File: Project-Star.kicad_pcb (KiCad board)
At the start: 2 copper layers, 95 parts, among them J1 Motor Driver Header, J10 Leg3 Motor1, J11 Leg4 Motor3, J12 Leg4 Motor2, J13 Leg4 Motor1, J14 Leg5 Motor3, J15 Leg5 Motor2, J16 Leg5 Motor1, J17 Leg6 Motor3, J18 Leg6 Motor2, J19 Leg6 Motor1, J2 Leg1 Motor3, J3 Leg1 Motor2, J4 Leg1 Motor1, J5 Leg2 Motor3, J6 Leg2 Motor2, J7 Leg2 Motor1, J8 Leg3 Motor3, J9 Leg3 Motor2, U1 PCA9685PW, U2 PCA9685PW, U3 LMR51625DDC, U4 LMR51450

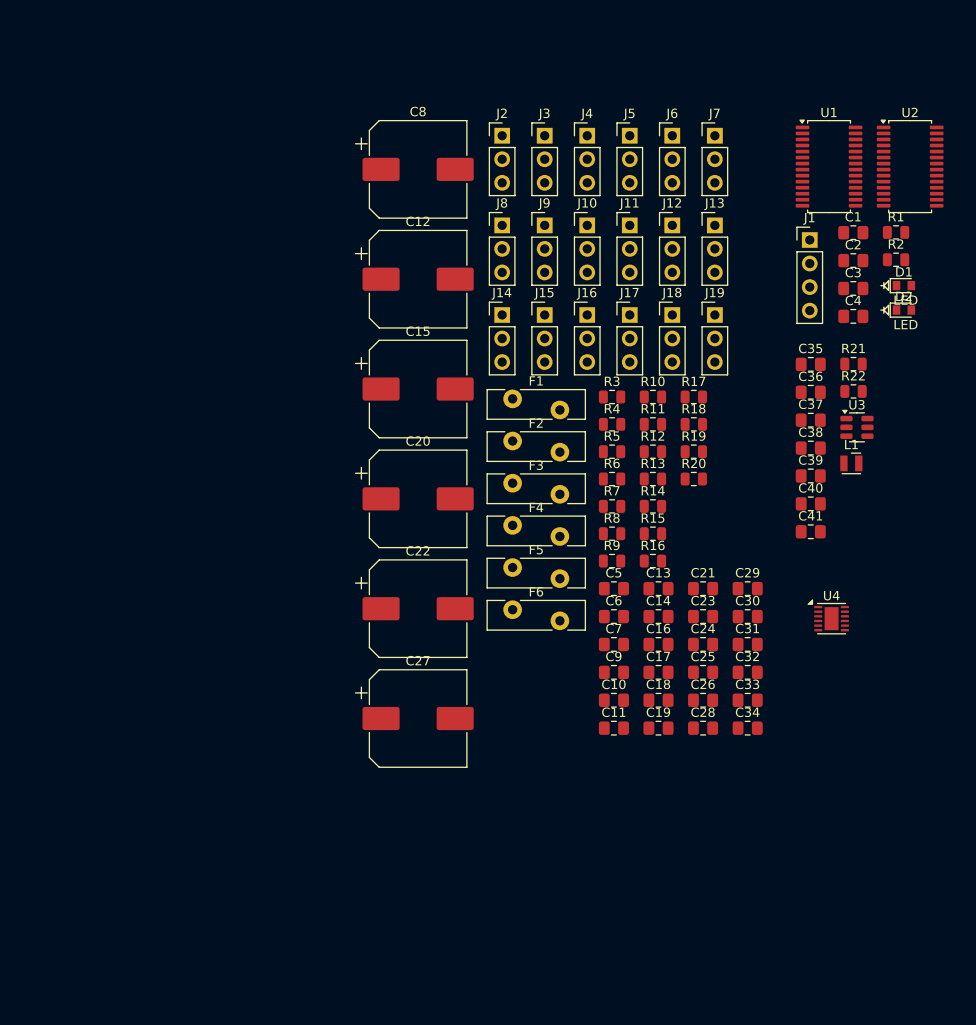
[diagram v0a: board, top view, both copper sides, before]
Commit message: added more power lines
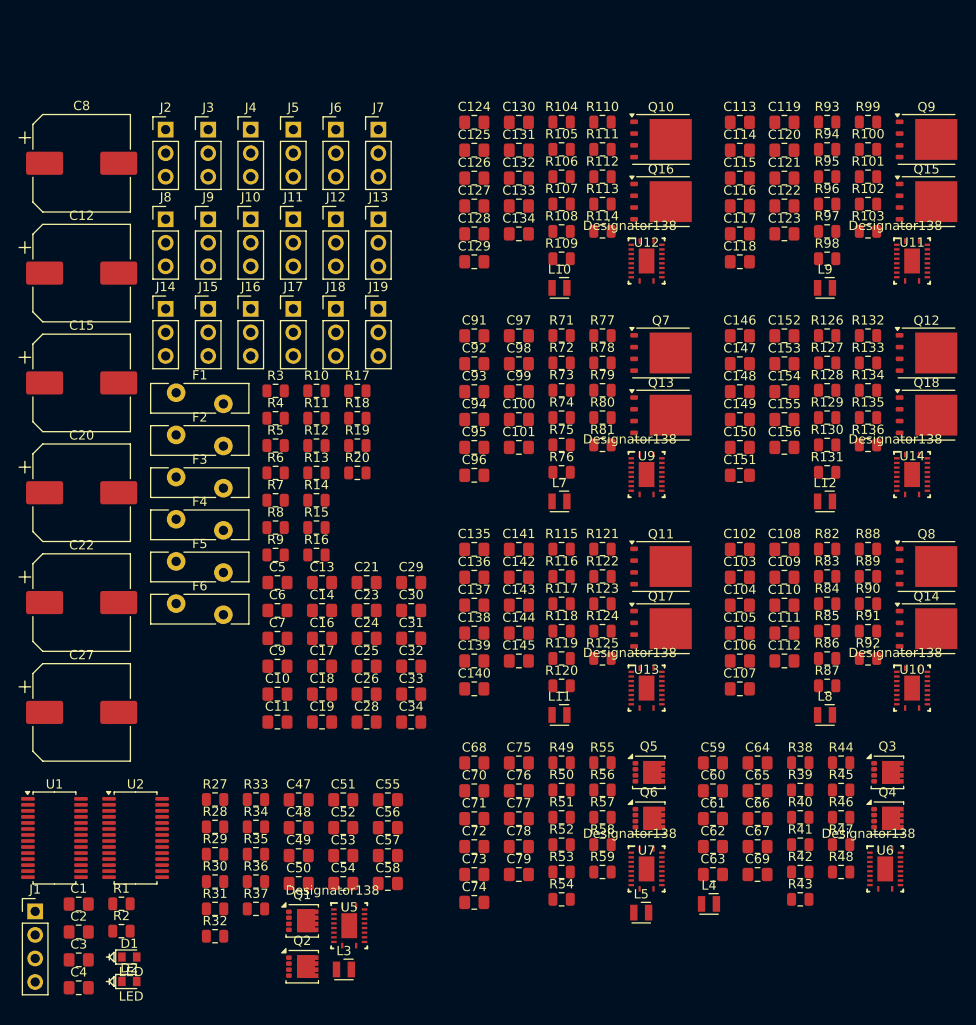
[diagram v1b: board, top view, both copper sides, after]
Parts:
- removed C35, C36: 4.7u, 3mOhm, Capacitor_SMD:C_0805_2012Metric_Pad1.18x1.45mm_HandSolder
- removed C37: 100n, 20mOhm, Capacitor_SMD:C_0805_2012Metric_Pad1.18x1.45mm_HandSolder
- removed C38: 100n, 1mOhm, Capacitor_SMD:C_0805_2012Metric_Pad1.18x1.45mm_HandSolder
- removed C39: 22p, 0Ohm, Capacitor_SMD:C_0805_2012Metric_Pad1.18x1.45mm_HandSolder
- removed C40, C41: 47u, 3.037mOhm, Capacitor_SMD:C_0805_2012Metric_Pad1.18x1.45mm_HandSolder
- removed L1: 8.2u, 45mOhm, Inductor_SMD_Wurth:L_Wurth_WE-LQSH-2010
- removed R21, R22: 150K_0603, PCM_4ms_Resistor:R_0805_2012Metric
- removed U3: LMR51625DDC, Package_TO_SOT_SMD:SOT-23-6
- removed U4: LMR51450, Package_SON:WSON-12-1EP_3x3mm_P0.5mm_EP1.5x2.5mm
- added C100: 10u, Capacitor_SMD:C_0805_2012Metric_Pad1.18x1.45mm_HandSolder, F.Cu at (143.8, 82.8)
- added C101: 10u, Capacitor_SMD:C_0805_2012Metric_Pad1.18x1.45mm_HandSolder, F.Cu at (143.8, 85.8)
- added C102: 4.7u, Capacitor_SMD:C_0805_2012Metric_Pad1.18x1.45mm_HandSolder, F.Cu at (167.7, 96.8)
- added C103: 56n, Capacitor_SMD:C_0805_2012Metric_Pad1.18x1.45mm_HandSolder, F.Cu at (167.7, 99.8)
- added C104: 2.2u, Capacitor_SMD:C_0805_2012Metric_Pad1.18x1.45mm_HandSolder, F.Cu at (167.7, 102.8)
- added C105: 100n, Capacitor_SMD:C_0805_2012Metric_Pad1.18x1.45mm_HandSolder, F.Cu at (167.7, 105.8)
- added C106: 10p, Capacitor_SMD:C_0805_2012Metric_Pad1.18x1.45mm_HandSolder, F.Cu at (167.7, 108.8)
- added C107: 100n, Capacitor_SMD:C_0805_2012Metric_Pad1.18x1.45mm_HandSolder, F.Cu at (167.7, 111.8)
- added C108: 8.2n, Capacitor_SMD:C_0805_2012Metric_Pad1.18x1.45mm_HandSolder, F.Cu at (172.5, 96.8)
- added C109: 680p, Capacitor_SMD:C_0805_2012Metric_Pad1.18x1.45mm_HandSolder, F.Cu at (172.5, 99.8)
- added C110: 470p, Capacitor_SMD:C_0805_2012Metric_Pad1.18x1.45mm_HandSolder, F.Cu at (172.5, 102.8)
- added C111: 10u, Capacitor_SMD:C_0805_2012Metric_Pad1.18x1.45mm_HandSolder, F.Cu at (172.5, 105.8)
- added C112: 10u, Capacitor_SMD:C_0805_2012Metric_Pad1.18x1.45mm_HandSolder, F.Cu at (172.5, 108.8)
- added C113: 4.7u, Capacitor_SMD:C_0805_2012Metric_Pad1.18x1.45mm_HandSolder, F.Cu at (167.7, 50.7)
- added C114: 56n, Capacitor_SMD:C_0805_2012Metric_Pad1.18x1.45mm_HandSolder, F.Cu at (167.7, 53.7)
- added C115: 2.2u, Capacitor_SMD:C_0805_2012Metric_Pad1.18x1.45mm_HandSolder, F.Cu at (167.7, 56.7)
- added C116: 100n, Capacitor_SMD:C_0805_2012Metric_Pad1.18x1.45mm_HandSolder, F.Cu at (167.7, 59.7)
- added C117: 10p, Capacitor_SMD:C_0805_2012Metric_Pad1.18x1.45mm_HandSolder, F.Cu at (167.7, 62.7)
- added C118: 100n, Capacitor_SMD:C_0805_2012Metric_Pad1.18x1.45mm_HandSolder, F.Cu at (167.7, 65.7)
- added C119: 8.2n, Capacitor_SMD:C_0805_2012Metric_Pad1.18x1.45mm_HandSolder, F.Cu at (172.5, 50.7)
- added C120: 680p, Capacitor_SMD:C_0805_2012Metric_Pad1.18x1.45mm_HandSolder, F.Cu at (172.5, 53.7)
- added C121: 470p, Capacitor_SMD:C_0805_2012Metric_Pad1.18x1.45mm_HandSolder, F.Cu at (172.5, 56.7)
- added C122: 10u, Capacitor_SMD:C_0805_2012Metric_Pad1.18x1.45mm_HandSolder, F.Cu at (172.5, 59.7)
- added C123: 10u, Capacitor_SMD:C_0805_2012Metric_Pad1.18x1.45mm_HandSolder, F.Cu at (172.5, 62.7)
- added C124: 4.7u, Capacitor_SMD:C_0805_2012Metric_Pad1.18x1.45mm_HandSolder, F.Cu at (139.0, 50.7)
- added C125: 56n, Capacitor_SMD:C_0805_2012Metric_Pad1.18x1.45mm_HandSolder, F.Cu at (139.0, 53.7)
- added C126: 2.2u, Capacitor_SMD:C_0805_2012Metric_Pad1.18x1.45mm_HandSolder, F.Cu at (139.0, 56.7)
- added C127: 100n, Capacitor_SMD:C_0805_2012Metric_Pad1.18x1.45mm_HandSolder, F.Cu at (139.0, 59.7)
- added C128: 10p, Capacitor_SMD:C_0805_2012Metric_Pad1.18x1.45mm_HandSolder, F.Cu at (139.0, 62.7)
- added C129: 100n, Capacitor_SMD:C_0805_2012Metric_Pad1.18x1.45mm_HandSolder, F.Cu at (139.0, 65.7)
- added C130: 8.2n, Capacitor_SMD:C_0805_2012Metric_Pad1.18x1.45mm_HandSolder, F.Cu at (143.8, 50.7)
- added C131: 680p, Capacitor_SMD:C_0805_2012Metric_Pad1.18x1.45mm_HandSolder, F.Cu at (143.8, 53.7)
- added C132: 470p, Capacitor_SMD:C_0805_2012Metric_Pad1.18x1.45mm_HandSolder, F.Cu at (143.8, 56.7)
- added C133: 10u, Capacitor_SMD:C_0805_2012Metric_Pad1.18x1.45mm_HandSolder, F.Cu at (143.8, 59.7)
- added C134: 10u, Capacitor_SMD:C_0805_2012Metric_Pad1.18x1.45mm_HandSolder, F.Cu at (143.8, 62.7)
- added C135: 4.7u, Capacitor_SMD:C_0805_2012Metric_Pad1.18x1.45mm_HandSolder, F.Cu at (139.0, 96.8)
- added C136: 56n, Capacitor_SMD:C_0805_2012Metric_Pad1.18x1.45mm_HandSolder, F.Cu at (139.0, 99.8)
- added C137: 2.2u, Capacitor_SMD:C_0805_2012Metric_Pad1.18x1.45mm_HandSolder, F.Cu at (139.0, 102.8)
- added C138: 100n, Capacitor_SMD:C_0805_2012Metric_Pad1.18x1.45mm_HandSolder, F.Cu at (139.0, 105.8)
- added C139: 10p, Capacitor_SMD:C_0805_2012Metric_Pad1.18x1.45mm_HandSolder, F.Cu at (139.0, 108.8)
- added C140: 100n, Capacitor_SMD:C_0805_2012Metric_Pad1.18x1.45mm_HandSolder, F.Cu at (139.0, 111.8)
- added C141: 8.2n, Capacitor_SMD:C_0805_2012Metric_Pad1.18x1.45mm_HandSolder, F.Cu at (143.8, 96.8)
- added C142: 680p, Capacitor_SMD:C_0805_2012Metric_Pad1.18x1.45mm_HandSolder, F.Cu at (143.8, 99.8)
- added C143: 470p, Capacitor_SMD:C_0805_2012Metric_Pad1.18x1.45mm_HandSolder, F.Cu at (143.8, 102.8)
- added C144: 10u, Capacitor_SMD:C_0805_2012Metric_Pad1.18x1.45mm_HandSolder, F.Cu at (143.8, 105.8)
- added C145: 10u, Capacitor_SMD:C_0805_2012Metric_Pad1.18x1.45mm_HandSolder, F.Cu at (143.8, 108.8)
- added C146: 4.7u, Capacitor_SMD:C_0805_2012Metric_Pad1.18x1.45mm_HandSolder, F.Cu at (167.7, 73.7)
- added C147: 56n, Capacitor_SMD:C_0805_2012Metric_Pad1.18x1.45mm_HandSolder, F.Cu at (167.7, 76.7)
- added C148: 2.2u, Capacitor_SMD:C_0805_2012Metric_Pad1.18x1.45mm_HandSolder, F.Cu at (167.7, 79.8)
- added C149: 100n, Capacitor_SMD:C_0805_2012Metric_Pad1.18x1.45mm_HandSolder, F.Cu at (167.7, 82.8)
- added C150: 10p, Capacitor_SMD:C_0805_2012Metric_Pad1.18x1.45mm_HandSolder, F.Cu at (167.7, 85.8)
- added C151: 100n, Capacitor_SMD:C_0805_2012Metric_Pad1.18x1.45mm_HandSolder, F.Cu at (167.7, 88.8)
- added C152: 8.2n, Capacitor_SMD:C_0805_2012Metric_Pad1.18x1.45mm_HandSolder, F.Cu at (172.5, 73.7)
- added C153: 680p, Capacitor_SMD:C_0805_2012Metric_Pad1.18x1.45mm_HandSolder, F.Cu at (172.5, 76.7)
- added C154: 470p, Capacitor_SMD:C_0805_2012Metric_Pad1.18x1.45mm_HandSolder, F.Cu at (172.5, 79.8)
- added C155: 10u, Capacitor_SMD:C_0805_2012Metric_Pad1.18x1.45mm_HandSolder, F.Cu at (172.5, 82.8)
- added C156: 10u, Capacitor_SMD:C_0805_2012Metric_Pad1.18x1.45mm_HandSolder, F.Cu at (172.5, 85.8)
- added C47: 4.7u, Capacitor_SMD:C_0805_2012Metric_Pad1.18x1.45mm_HandSolder, F.Cu at (120.1, 123.8)
- added C48: 56n, Capacitor_SMD:C_0805_2012Metric_Pad1.18x1.45mm_HandSolder, F.Cu at (120.1, 126.8)
- added C49: 2.2u, Capacitor_SMD:C_0805_2012Metric_Pad1.18x1.45mm_HandSolder, F.Cu at (120.1, 129.8)
- added C50: 100n, Capacitor_SMD:C_0805_2012Metric_Pad1.18x1.45mm_HandSolder, F.Cu at (120.1, 132.8)
- added C51: 5.1p, Capacitor_SMD:C_0805_2012Metric_Pad1.18x1.45mm_HandSolder, F.Cu at (124.9, 123.8)
- added C52: 100n, Capacitor_SMD:C_0805_2012Metric_Pad1.18x1.45mm_HandSolder, F.Cu at (124.9, 126.8)
- added C53: 8.2n, Capacitor_SMD:C_0805_2012Metric_Pad1.18x1.45mm_HandSolder, F.Cu at (124.9, 129.8)
- added C54: 560p, Capacitor_SMD:C_0805_2012Metric_Pad1.18x1.45mm_HandSolder, F.Cu at (124.9, 132.8)
- added C55: 10u, Capacitor_SMD:C_0805_2012Metric_Pad1.18x1.45mm_HandSolder, F.Cu at (129.7, 123.8)
- added C56: 10u, Capacitor_SMD:C_0805_2012Metric_Pad1.18x1.45mm_HandSolder, F.Cu at (129.7, 126.8)
- added C57: 680p, Capacitor_SMD:C_0805_2012Metric_Pad1.18x1.45mm_HandSolder, F.Cu at (129.7, 129.8)
- added C58: 10u, Capacitor_SMD:C_0805_2012Metric_Pad1.18x1.45mm_HandSolder, F.Cu at (129.7, 132.8)
- added C59: 10u, Capacitor_SMD:C_0805_2012Metric_Pad1.18x1.45mm_HandSolder, F.Cu at (164.8, 119.8)
- added C60: 56n, Capacitor_SMD:C_0805_2012Metric_Pad1.18x1.45mm_HandSolder, F.Cu at (164.8, 122.8)
- added C61: 2.2u, Capacitor_SMD:C_0805_2012Metric_Pad1.18x1.45mm_HandSolder, F.Cu at (164.8, 125.8)
- added C62: 100n, Capacitor_SMD:C_0805_2012Metric_Pad1.18x1.45mm_HandSolder, F.Cu at (164.8, 128.8)
- added C63: 3p, Capacitor_SMD:C_0805_2012Metric_Pad1.18x1.45mm_HandSolder, F.Cu at (164.8, 131.9)
- added C64: 100n, Capacitor_SMD:C_0805_2012Metric_Pad1.18x1.45mm_HandSolder, F.Cu at (169.6, 119.8)
- added C65: 8.2n, Capacitor_SMD:C_0805_2012Metric_Pad1.18x1.45mm_HandSolder, F.Cu at (169.6, 122.8)
- added C66: 470p, Capacitor_SMD:C_0805_2012Metric_Pad1.18x1.45mm_HandSolder, F.Cu at (169.6, 125.8)
- added C67: 47u, Capacitor_SMD:C_0805_2012Metric_Pad1.18x1.45mm_HandSolder, F.Cu at (169.6, 128.8)
- added C68: 4.7u, Capacitor_SMD:C_0805_2012Metric_Pad1.18x1.45mm_HandSolder, F.Cu at (139.0, 119.8)
- added C69: 750p, Capacitor_SMD:C_0805_2012Metric_Pad1.18x1.45mm_HandSolder, F.Cu at (169.6, 131.9)
- added C70: 56n, Capacitor_SMD:C_0805_2012Metric_Pad1.18x1.45mm_HandSolder, F.Cu at (139.0, 122.8)
- added C71: 2.2u, Capacitor_SMD:C_0805_2012Metric_Pad1.18x1.45mm_HandSolder, F.Cu at (139.0, 125.8)
- added C72: 100n, Capacitor_SMD:C_0805_2012Metric_Pad1.18x1.45mm_HandSolder, F.Cu at (139.0, 128.8)
- added C73: 2p, Capacitor_SMD:C_0805_2012Metric_Pad1.18x1.45mm_HandSolder, F.Cu at (139.0, 131.9)
- added C74: 100n, Capacitor_SMD:C_0805_2012Metric_Pad1.18x1.45mm_HandSolder, F.Cu at (139.0, 134.9)
- added C75: 8.2n, Capacitor_SMD:C_0805_2012Metric_Pad1.18x1.45mm_HandSolder, F.Cu at (143.8, 119.8)
- added C76: 470p, Capacitor_SMD:C_0805_2012Metric_Pad1.18x1.45mm_HandSolder, F.Cu at (143.8, 122.8)
- added C77: 820p, Capacitor_SMD:C_0805_2012Metric_Pad1.18x1.45mm_HandSolder, F.Cu at (143.8, 125.8)
- added C78: 10u, Capacitor_SMD:C_0805_2012Metric_Pad1.18x1.45mm_HandSolder, F.Cu at (143.8, 128.8)
- added C79: 10u, Capacitor_SMD:C_0805_2012Metric_Pad1.18x1.45mm_HandSolder, F.Cu at (143.8, 131.9)
- added C91: 4.7u, Capacitor_SMD:C_0805_2012Metric_Pad1.18x1.45mm_HandSolder, F.Cu at (139.0, 73.7)
- added C92: 56n, Capacitor_SMD:C_0805_2012Metric_Pad1.18x1.45mm_HandSolder, F.Cu at (139.0, 76.7)
- added C93: 2.2u, Capacitor_SMD:C_0805_2012Metric_Pad1.18x1.45mm_HandSolder, F.Cu at (139.0, 79.8)
- added C94: 100n, Capacitor_SMD:C_0805_2012Metric_Pad1.18x1.45mm_HandSolder, F.Cu at (139.0, 82.8)
- added C95: 10p, Capacitor_SMD:C_0805_2012Metric_Pad1.18x1.45mm_HandSolder, F.Cu at (139.0, 85.8)
- added C96: 100n, Capacitor_SMD:C_0805_2012Metric_Pad1.18x1.45mm_HandSolder, F.Cu at (139.0, 88.8)
- added C97: 8.2n, Capacitor_SMD:C_0805_2012Metric_Pad1.18x1.45mm_HandSolder, F.Cu at (143.8, 73.7)
- added C98: 680p, Capacitor_SMD:C_0805_2012Metric_Pad1.18x1.45mm_HandSolder, F.Cu at (143.8, 76.7)
- added C99: 470p, Capacitor_SMD:C_0805_2012Metric_Pad1.18x1.45mm_HandSolder, F.Cu at (143.8, 79.8)
- added L10: 4.7u, Inductor_SMD_Wurth:L_Wurth_WE-LQSH-2010, F.Cu at (148.2, 68.6)
- added L11: 4.7u, Inductor_SMD_Wurth:L_Wurth_WE-LQSH-2010, F.Cu at (148.2, 114.6)
- added L12: 4.7u, Inductor_SMD_Wurth:L_Wurth_WE-LQSH-2010, F.Cu at (176.9, 91.6)
- added L3: 6.8u, Inductor_SMD_Wurth:L_Wurth_WE-LQSH-2010, F.Cu at (124.9, 142.1)
- added L4: 7.8u, Inductor_SMD_Wurth:L_Wurth_WE-LQSH-2010, F.Cu at (164.3, 135.0)
- added L5: 10u, Inductor_SMD_Wurth:L_Wurth_WE-LQSH-2010, F.Cu at (157.0, 136.0)
- added L7: 4.7u, Inductor_SMD_Wurth:L_Wurth_WE-LQSH-2010, F.Cu at (148.2, 91.6)
- added L8: 4.7u, Inductor_SMD_Wurth:L_Wurth_WE-LQSH-2010, F.Cu at (176.9, 114.6)
- added L9: 4.7u, Inductor_SMD_Wurth:L_Wurth_WE-LQSH-2010, F.Cu at (176.9, 68.6)
- added Q1: CSD18543Q3A, Package_SON:VSON-8_3.3x3.3mm_P0.65mm_NexFET, F.Cu at (120.5, 136.9)
- added Q10: CSD19502Q5B, Package_TO_SOT_SMD:TDSON-8-1, F.Cu at (159.2, 52.5)
- added Q11: CSD19502Q5B, Package_TO_SOT_SMD:TDSON-8-1, F.Cu at (159.2, 98.6)
- added Q12: CSD19502Q5B, Package_TO_SOT_SMD:TDSON-8-1, F.Cu at (187.8, 75.6)
- added Q13: CSD19502Q5B, Package_TO_SOT_SMD:TDSON-8-1, F.Cu at (159.2, 82.3)
- added Q14: CSD19502Q5B, Package_TO_SOT_SMD:TDSON-8-1, F.Cu at (187.8, 105.3)
- added Q15: CSD19502Q5B, Package_TO_SOT_SMD:TDSON-8-1, F.Cu at (187.8, 59.3)
- added Q16: CSD19502Q5B, Package_TO_SOT_SMD:TDSON-8-1, F.Cu at (159.2, 59.3)
- added Q17: CSD19502Q5B, Package_TO_SOT_SMD:TDSON-8-1, F.Cu at (159.2, 105.3)
- added Q18: CSD19502Q5B, Package_TO_SOT_SMD:TDSON-8-1, F.Cu at (187.8, 82.3)
- added Q2: CSD18543Q3A, Package_SON:VSON-8_3.3x3.3mm_P0.65mm_NexFET, F.Cu at (120.5, 141.8)
- added Q3: CSD18543Q3A, Package_SON:VSON-8_3.3x3.3mm_P0.65mm_NexFET, F.Cu at (183.6, 120.8)
- added Q4: CSD18543Q3A, Package_SON:VSON-8_3.3x3.3mm_P0.65mm_NexFET, F.Cu at (183.6, 125.8)
- added Q5: CSD18543Q3A, Package_SON:VSON-8_3.3x3.3mm_P0.65mm_NexFET, F.Cu at (157.8, 120.8)
- added Q6: CSD18543Q3A, Package_SON:VSON-8_3.3x3.3mm_P0.65mm_NexFET, F.Cu at (157.8, 125.8)
- added Q7: CSD19502Q5B, Package_TO_SOT_SMD:TDSON-8-1, F.Cu at (159.2, 75.6)
- added Q8: CSD19502Q5B, Package_TO_SOT_SMD:TDSON-8-1, F.Cu at (187.8, 98.6)
- added Q9: CSD19502Q5B, Package_TO_SOT_SMD:TDSON-8-1, F.Cu at (187.8, 52.5)
- added R100: 150K_0603, PCM_4ms_Resistor:R_0805_2012Metric, F.Cu at (181.5, 53.6)
- added R101: 150K_0603, PCM_4ms_Resistor:R_0805_2012Metric, F.Cu at (181.5, 56.6)
- added R102: 150K_0603, PCM_4ms_Resistor:R_0805_2012Metric, F.Cu at (181.5, 59.5)
- added R103: 150K_0603, PCM_4ms_Resistor:R_0805_2012Metric, F.Cu at (181.5, 62.5)
- added R104: 150K_0603, PCM_4ms_Resistor:R_0805_2012Metric, F.Cu at (148.4, 50.7)
- added R105: 150K_0603, PCM_4ms_Resistor:R_0805_2012Metric, F.Cu at (148.4, 53.6)
- added R106: 150K_0603, PCM_4ms_Resistor:R_0805_2012Metric, F.Cu at (148.4, 56.6)
- added R107: 150K_0603, PCM_4ms_Resistor:R_0805_2012Metric, F.Cu at (148.4, 59.5)
- added R108: 150K_0603, PCM_4ms_Resistor:R_0805_2012Metric, F.Cu at (148.4, 62.5)
- added R109: 150K_0603, PCM_4ms_Resistor:R_0805_2012Metric, F.Cu at (148.4, 65.4)
- added R110: 150K_0603, PCM_4ms_Resistor:R_0805_2012Metric, F.Cu at (152.8, 50.7)
- added R111: 150K_0603, PCM_4ms_Resistor:R_0805_2012Metric, F.Cu at (152.8, 53.6)
- added R112: 150K_0603, PCM_4ms_Resistor:R_0805_2012Metric, F.Cu at (152.8, 56.6)
- added R113: 150K_0603, PCM_4ms_Resistor:R_0805_2012Metric, F.Cu at (152.8, 59.5)
- added R114: 150K_0603, PCM_4ms_Resistor:R_0805_2012Metric, F.Cu at (152.8, 62.5)
- added R115: 150K_0603, PCM_4ms_Resistor:R_0805_2012Metric, F.Cu at (148.4, 96.7)
- added R116: 150K_0603, PCM_4ms_Resistor:R_0805_2012Metric, F.Cu at (148.4, 99.7)
- added R117: 150K_0603, PCM_4ms_Resistor:R_0805_2012Metric, F.Cu at (148.4, 102.6)
- added R118: 150K_0603, PCM_4ms_Resistor:R_0805_2012Metric, F.Cu at (148.4, 105.6)
- added R119: 150K_0603, PCM_4ms_Resistor:R_0805_2012Metric, F.Cu at (148.4, 108.5)
- added R120: 150K_0603, PCM_4ms_Resistor:R_0805_2012Metric, F.Cu at (148.4, 111.5)
- added R121: 150K_0603, PCM_4ms_Resistor:R_0805_2012Metric, F.Cu at (152.8, 96.7)
- added R122: 150K_0603, PCM_4ms_Resistor:R_0805_2012Metric, F.Cu at (152.8, 99.7)
- added R123: 150K_0603, PCM_4ms_Resistor:R_0805_2012Metric, F.Cu at (152.8, 102.6)
- added R124: 150K_0603, PCM_4ms_Resistor:R_0805_2012Metric, F.Cu at (152.8, 105.6)
- added R125: 150K_0603, PCM_4ms_Resistor:R_0805_2012Metric, F.Cu at (152.8, 108.5)
- added R126: 150K_0603, PCM_4ms_Resistor:R_0805_2012Metric, F.Cu at (177.1, 73.7)
- added R127: 150K_0603, PCM_4ms_Resistor:R_0805_2012Metric, F.Cu at (177.1, 76.7)
- added R128: 150K_0603, PCM_4ms_Resistor:R_0805_2012Metric, F.Cu at (177.1, 79.6)
- added R129: 150K_0603, PCM_4ms_Resistor:R_0805_2012Metric, F.Cu at (177.1, 82.6)
- added R130: 150K_0603, PCM_4ms_Resistor:R_0805_2012Metric, F.Cu at (177.1, 85.5)
- added R131: 150K_0603, PCM_4ms_Resistor:R_0805_2012Metric, F.Cu at (177.1, 88.5)
- added R132: 150K_0603, PCM_4ms_Resistor:R_0805_2012Metric, F.Cu at (181.5, 73.7)
- added R133: 150K_0603, PCM_4ms_Resistor:R_0805_2012Metric, F.Cu at (181.5, 76.7)
- added R134: 150K_0603, PCM_4ms_Resistor:R_0805_2012Metric, F.Cu at (181.5, 79.6)
- added R135: 150K_0603, PCM_4ms_Resistor:R_0805_2012Metric, F.Cu at (181.5, 82.6)
- added R136: 150K_0603, PCM_4ms_Resistor:R_0805_2012Metric, F.Cu at (181.5, 85.5)
- added R27: 150K_0603, PCM_4ms_Resistor:R_0805_2012Metric, F.Cu at (111.0, 123.8)
- added R28: 150K_0603, PCM_4ms_Resistor:R_0805_2012Metric, F.Cu at (111.0, 126.7)
- added R29: 150K_0603, PCM_4ms_Resistor:R_0805_2012Metric, F.Cu at (111.0, 129.7)
- added R30: 150K_0603, PCM_4ms_Resistor:R_0805_2012Metric, F.Cu at (111.0, 132.6)
- added R31: 150K_0603, PCM_4ms_Resistor:R_0805_2012Metric, F.Cu at (111.0, 135.6)
- added R32: 150K_0603, PCM_4ms_Resistor:R_0805_2012Metric, F.Cu at (111.0, 138.5)
- added R33: 150K_0603, PCM_4ms_Resistor:R_0805_2012Metric, F.Cu at (115.5, 123.8)
- added R34: 150K_0603, PCM_4ms_Resistor:R_0805_2012Metric, F.Cu at (115.5, 126.7)
- added R35: 150K_0603, PCM_4ms_Resistor:R_0805_2012Metric, F.Cu at (115.5, 129.7)
- added R36: 150K_0603, PCM_4ms_Resistor:R_0805_2012Metric, F.Cu at (115.5, 132.6)
- added R37: 150K_0603, PCM_4ms_Resistor:R_0805_2012Metric, F.Cu at (115.5, 135.6)
- added R38: 150K_0603, PCM_4ms_Resistor:R_0805_2012Metric, F.Cu at (174.2, 119.8)
- added R39: 150K_0603, PCM_4ms_Resistor:R_0805_2012Metric, F.Cu at (174.2, 122.7)
- added R40: 150K_0603, PCM_4ms_Resistor:R_0805_2012Metric, F.Cu at (174.2, 125.7)
- added R41: 150K_0603, PCM_4ms_Resistor:R_0805_2012Metric, F.Cu at (174.2, 128.6)
- added R42: 150K_0603, PCM_4ms_Resistor:R_0805_2012Metric, F.Cu at (174.2, 131.6)
- added R43: 150K_0603, PCM_4ms_Resistor:R_0805_2012Metric, F.Cu at (174.2, 134.5)
- added R44: 150K_0603, PCM_4ms_Resistor:R_0805_2012Metric, F.Cu at (178.6, 119.8)
- added R45: 150K_0603, PCM_4ms_Resistor:R_0805_2012Metric, F.Cu at (178.6, 122.7)
- added R46: 150K_0603, PCM_4ms_Resistor:R_0805_2012Metric, F.Cu at (178.6, 125.7)
- added R47: 150K_0603, PCM_4ms_Resistor:R_0805_2012Metric, F.Cu at (178.6, 128.6)
- added R48: 150K_0603, PCM_4ms_Resistor:R_0805_2012Metric, F.Cu at (178.6, 131.6)
- added R49: 150K_0603, PCM_4ms_Resistor:R_0805_2012Metric, F.Cu at (148.4, 119.8)
- added R50: 150K_0603, PCM_4ms_Resistor:R_0805_2012Metric, F.Cu at (148.4, 122.7)
- added R51: 150K_0603, PCM_4ms_Resistor:R_0805_2012Metric, F.Cu at (148.4, 125.7)
- added R52: 150K_0603, PCM_4ms_Resistor:R_0805_2012Metric, F.Cu at (148.4, 128.6)
- added R53: 150K_0603, PCM_4ms_Resistor:R_0805_2012Metric, F.Cu at (148.4, 131.6)
- added R54: 150K_0603, PCM_4ms_Resistor:R_0805_2012Metric, F.Cu at (148.4, 134.5)
- added R55: 150K_0603, PCM_4ms_Resistor:R_0805_2012Metric, F.Cu at (152.8, 119.8)
- added R56: 150K_0603, PCM_4ms_Resistor:R_0805_2012Metric, F.Cu at (152.8, 122.7)
- added R57: 150K_0603, PCM_4ms_Resistor:R_0805_2012Metric, F.Cu at (152.8, 125.7)
- added R58: 150K_0603, PCM_4ms_Resistor:R_0805_2012Metric, F.Cu at (152.8, 128.6)
- added R59: 150K_0603, PCM_4ms_Resistor:R_0805_2012Metric, F.Cu at (152.8, 131.6)
- added R71: 150K_0603, PCM_4ms_Resistor:R_0805_2012Metric, F.Cu at (148.4, 73.7)
- added R72: 150K_0603, PCM_4ms_Resistor:R_0805_2012Metric, F.Cu at (148.4, 76.7)
- added R73: 150K_0603, PCM_4ms_Resistor:R_0805_2012Metric, F.Cu at (148.4, 79.6)
- added R74: 150K_0603, PCM_4ms_Resistor:R_0805_2012Metric, F.Cu at (148.4, 82.6)
- added R75: 150K_0603, PCM_4ms_Resistor:R_0805_2012Metric, F.Cu at (148.4, 85.5)
- added R76: 150K_0603, PCM_4ms_Resistor:R_0805_2012Metric, F.Cu at (148.4, 88.5)
- added R77: 150K_0603, PCM_4ms_Resistor:R_0805_2012Metric, F.Cu at (152.8, 73.7)
- added R78: 150K_0603, PCM_4ms_Resistor:R_0805_2012Metric, F.Cu at (152.8, 76.7)
- added R79: 150K_0603, PCM_4ms_Resistor:R_0805_2012Metric, F.Cu at (152.8, 79.6)
- added R80: 150K_0603, PCM_4ms_Resistor:R_0805_2012Metric, F.Cu at (152.8, 82.6)
- added R81: 150K_0603, PCM_4ms_Resistor:R_0805_2012Metric, F.Cu at (152.8, 85.5)
- added R82: 150K_0603, PCM_4ms_Resistor:R_0805_2012Metric, F.Cu at (177.1, 96.7)
- added R83: 150K_0603, PCM_4ms_Resistor:R_0805_2012Metric, F.Cu at (177.1, 99.7)
- added R84: 150K_0603, PCM_4ms_Resistor:R_0805_2012Metric, F.Cu at (177.1, 102.6)
- added R85: 150K_0603, PCM_4ms_Resistor:R_0805_2012Metric, F.Cu at (177.1, 105.6)
- added R86: 150K_0603, PCM_4ms_Resistor:R_0805_2012Metric, F.Cu at (177.1, 108.5)
- added R87: 150K_0603, PCM_4ms_Resistor:R_0805_2012Metric, F.Cu at (177.1, 111.5)
- added R88: 150K_0603, PCM_4ms_Resistor:R_0805_2012Metric, F.Cu at (181.5, 96.7)
- added R89: 150K_0603, PCM_4ms_Resistor:R_0805_2012Metric, F.Cu at (181.5, 99.7)
- added R90: 150K_0603, PCM_4ms_Resistor:R_0805_2012Metric, F.Cu at (181.5, 102.6)
- added R91: 150K_0603, PCM_4ms_Resistor:R_0805_2012Metric, F.Cu at (181.5, 105.6)
- added R92: 150K_0603, PCM_4ms_Resistor:R_0805_2012Metric, F.Cu at (181.5, 108.5)
- added R93: 150K_0603, PCM_4ms_Resistor:R_0805_2012Metric, F.Cu at (177.1, 50.7)
- added R94: 150K_0603, PCM_4ms_Resistor:R_0805_2012Metric, F.Cu at (177.1, 53.6)
- added R95: 150K_0603, PCM_4ms_Resistor:R_0805_2012Metric, F.Cu at (177.1, 56.6)
- added R96: 150K_0603, PCM_4ms_Resistor:R_0805_2012Metric, F.Cu at (177.1, 59.5)
- added R97: 150K_0603, PCM_4ms_Resistor:R_0805_2012Metric, F.Cu at (177.1, 62.5)
- added R98: 150K_0603, PCM_4ms_Resistor:R_0805_2012Metric, F.Cu at (177.1, 65.4)
- added R99: 150K_0603, PCM_4ms_Resistor:R_0805_2012Metric, F.Cu at (181.5, 50.7)
- added U10: LM25145RGYR, Project_Star_Regulator_Switching:RGY0020B, F.Cu at (186.3, 111.7)
- added U11: LM25145RGYR, Project_Star_Regulator_Switching:RGY0020B, F.Cu at (186.3, 65.7)
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
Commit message: 20V line PCB v1
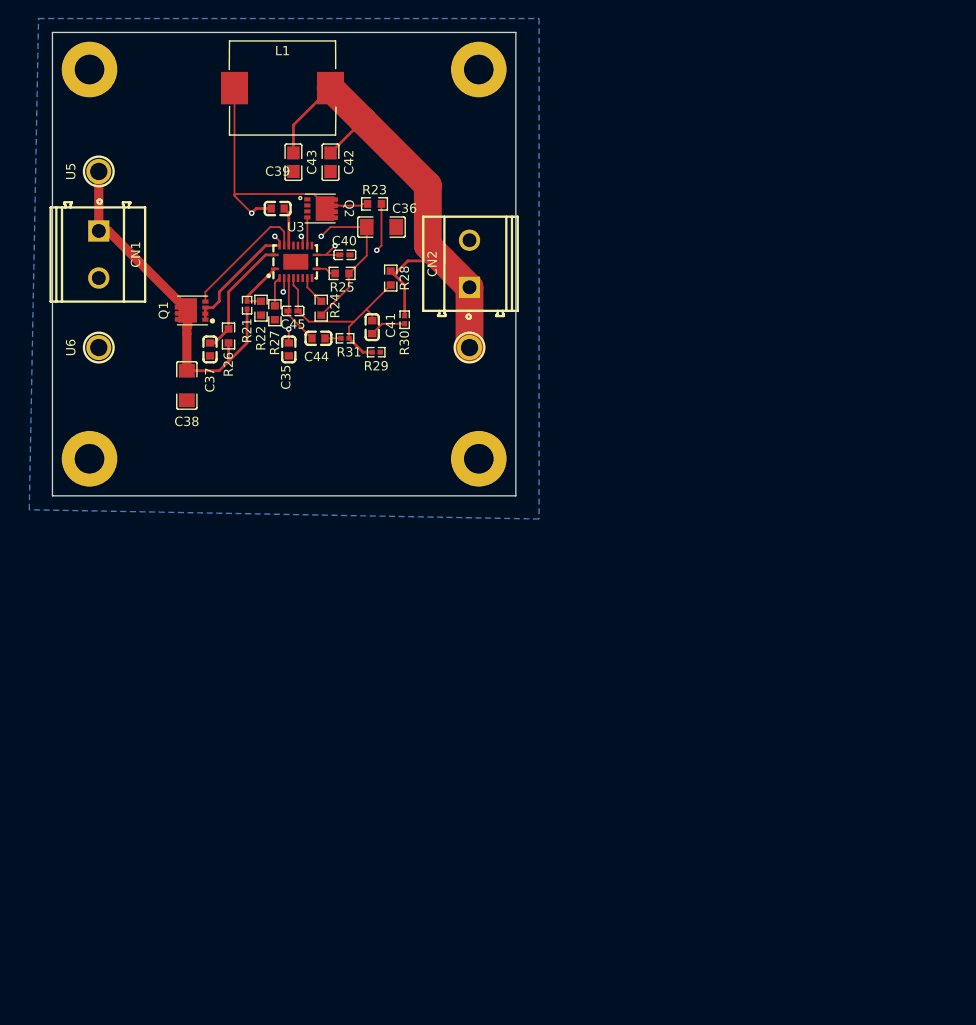
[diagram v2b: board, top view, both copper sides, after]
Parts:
- removed C1, C3: 0.1u, Capacitor_SMD:C_0805_2012Metric_Pad1.18x1.45mm_HandSolder
- removed C10, C100, C101, C11, C111, C112, C122, C123, C13, C133, C134, C14, C144, C145, C155, C156, C16, C17, C18, C19, C2, C21, C23, C24, C25, C26, C28, C29, C30, C31, C32, C33, C34, C4, C5, C55, C56, C58, C59, C6, C7, C78, C79, C9: 10u, Capacitor_SMD:C_0805_2012Metric_Pad1.18x1.45mm_HandSolder
- removed C102, C113, C124, C135, C146, C47, C68, C91: 4.7u, Capacitor_SMD:C_0805_2012Metric_Pad1.18x1.45mm_HandSolder
- removed C103, C114, C125, C136, C147, C48, C60, C70, C92: 56n, Capacitor_SMD:C_0805_2012Metric_Pad1.18x1.45mm_HandSolder
- removed C104, C115, C126, C137, C148, C49, C61, C71, C93: 2.2u, Capacitor_SMD:C_0805_2012Metric_Pad1.18x1.45mm_HandSolder
- removed C105, C107, C116, C118, C127, C129, C138, C140, C149, C151, C50, C52, C62, C64, C72, C74, C94, C96: 100n, Capacitor_SMD:C_0805_2012Metric_Pad1.18x1.45mm_HandSolder
- removed C106, C117, C128, C139, C150, C95: 10p, Capacitor_SMD:C_0805_2012Metric_Pad1.18x1.45mm_HandSolder
- removed C108, C119, C130, C141, C152, C53, C65, C75, C97: 8.2n, Capacitor_SMD:C_0805_2012Metric_Pad1.18x1.45mm_HandSolder
- removed C109, C120, C131, C142, C153, C57, C98: 680p, Capacitor_SMD:C_0805_2012Metric_Pad1.18x1.45mm_HandSolder
- removed C110, C121, C132, C143, C154, C66, C76, C99: 470p, Capacitor_SMD:C_0805_2012Metric_Pad1.18x1.45mm_HandSolder
- removed C12, C15, C20, C22, C27, C8: 1000u, Capacitor_SMD:CP_Elec_10x10
- removed C51: 5.1p, Capacitor_SMD:C_0805_2012Metric_Pad1.18x1.45mm_HandSolder
- removed C54: 560p, Capacitor_SMD:C_0805_2012Metric_Pad1.18x1.45mm_HandSolder
- removed C63: 3p, Capacitor_SMD:C_0805_2012Metric_Pad1.18x1.45mm_HandSolder
- removed C67: 47u, Capacitor_SMD:C_0805_2012Metric_Pad1.18x1.45mm_HandSolder
- removed C69: 750p, Capacitor_SMD:C_0805_2012Metric_Pad1.18x1.45mm_HandSolder
- removed C73: 2p, Capacitor_SMD:C_0805_2012Metric_Pad1.18x1.45mm_HandSolder
- removed C77: 820p, Capacitor_SMD:C_0805_2012Metric_Pad1.18x1.45mm_HandSolder
- removed D1, D2: LED, PCM_4ms_LED:LED_0603_1608Metric
- removed F1, F2, F3, F4, F5, F6: MF-RG500, Fuse:Fuse_Bourns_MF-RG500
- removed J1: Motor Driver Header, Connector_PinHeader_2.54mm:PinHeader_1x04_P2.54mm_Vertical
- removed J10: Leg3 Motor1, Connector_PinHeader_2.54mm:PinHeader_1x03_P2.54mm_Vertical
- removed J11: Leg4 Motor3, Connector_PinHeader_2.54mm:PinHeader_1x03_P2.54mm_Vertical
- removed J12: Leg4 Motor2, Connector_PinHeader_2.54mm:PinHeader_1x03_P2.54mm_Vertical
- removed J13: Leg4 Motor1, Connector_PinHeader_2.54mm:PinHeader_1x03_P2.54mm_Vertical
- removed J14: Leg5 Motor3, Connector_PinHeader_2.54mm:PinHeader_1x03_P2.54mm_Vertical
- removed J15: Leg5 Motor2, Connector_PinHeader_2.54mm:PinHeader_1x03_P2.54mm_Vertical
- removed J16: Leg5 Motor1, Connector_PinHeader_2.54mm:PinHeader_1x03_P2.54mm_Vertical
- removed J17: Leg6 Motor3, Connector_PinHeader_2.54mm:PinHeader_1x03_P2.54mm_Vertical
- removed J18: Leg6 Motor2, Connector_PinHeader_2.54mm:PinHeader_1x03_P2.54mm_Vertical
- removed J19: Leg6 Motor1, Connector_PinHeader_2.54mm:PinHeader_1x03_P2.54mm_Vertical
- removed J2: Leg1 Motor3, Connector_PinHeader_2.54mm:PinHeader_1x03_P2.54mm_Vertical
- removed J3: Leg1 Motor2, Connector_PinHeader_2.54mm:PinHeader_1x03_P2.54mm_Vertical
- removed J4: Leg1 Motor1, Connector_PinHeader_2.54mm:PinHeader_1x03_P2.54mm_Vertical
- removed J5: Leg2 Motor3, Connector_PinHeader_2.54mm:PinHeader_1x03_P2.54mm_Vertical
- removed J6: Leg2 Motor2, Connector_PinHeader_2.54mm:PinHeader_1x03_P2.54mm_Vertical
- removed J7: Leg2 Motor1, Connector_PinHeader_2.54mm:PinHeader_1x03_P2.54mm_Vertical
- removed J8: Leg3 Motor3, Connector_PinHeader_2.54mm:PinHeader_1x03_P2.54mm_Vertical
- removed J9: Leg3 Motor2, Connector_PinHeader_2.54mm:PinHeader_1x03_P2.54mm_Vertical
- removed L10, L11, L12, L7, L8, L9: 4.7u, Inductor_SMD_Wurth:L_Wurth_WE-LQSH-2010
- removed L3: 6.8u, Inductor_SMD_Wurth:L_Wurth_WE-LQSH-2010
- removed L4: 7.8u, Inductor_SMD_Wurth:L_Wurth_WE-LQSH-2010
- removed L5: 10u, Inductor_SMD_Wurth:L_Wurth_WE-LQSH-2010
- removed Q10, Q11, Q12, Q13, Q14, Q15, Q16, Q17, Q18, Q7, Q8, Q9: CSD19502Q5B, Package_TO_SOT_SMD:TDSON-8-1
- removed Q3, Q4, Q5, Q6: CSD18543Q3A, Package_SON:VSON-8_3.3x3.3mm_P0.65mm_NexFET
- removed R1, R10, R100, R101, R102, R103, R104, R105, R106, R107, R108, R109, R11, R110, R111, R112, R113, R114, R115, R116, R117, R118, R119, R12, R120, R121, R122, R123, R124, R125, R126, R127, R128, R129, R13, R130, R131, R132, R133, R134, R135, R136, R14, R15, R16, R17, R18, R19, R2, R20, R3, R32, R33, R34, R35, R36, R37, R38, R39, R4, R40, R41, R42, R43, R44, R45, R46, R47, R48, R49, R5, R50, R51, R52, R53, R54, R55, R56, R57, R58, R59, R6, R7, R71, R72, R73, R74, R75, R76, R77, R78, R79, R8, R80, R81, R82, R83, R84, R85, R86, R87, R88, R89, R9, R90, R91, R92, R93, R94, R95, R96, R97, R98, R99: 150K_0603, PCM_4ms_Resistor:R_0805_2012Metric
- removed U1, U2: PCA9685PW, Package_SO:TSSOP-28_4.4x9.7mm_P0.65mm
- removed U10, U11, U12, U13, U14, U7, U9: LM25145RGYR, Project_Star_Regulator_Switching:RGY0020B
- added C35: 39n, easyeda2kicad:C0603, F.Cu at (119.0, 75.2)
- added C36: 2.2u, easyeda2kicad:C1206, F.Cu at (129.0, 62.0)
- added C37: 100n, easyeda2kicad:C0603, F.Cu at (110.5, 75.2)
- added C38: 4.7u, easyeda2kicad:C1206, F.Cu at (108.0, 79.1)
- added C39: 100n, easyeda2kicad:C0603, F.Cu at (117.8, 60.0)
- added C40: 5.1p, easyeda2kicad:C0402, F.Cu at (125.0, 65.0)
- added C41: 390p, easyeda2kicad:C0603, F.Cu at (128.0, 72.8)
- added C42: 10u, easyeda2kicad:C0805, F.Cu at (123.5, 55.0)
- added C43: 10u, easyeda2kicad:C0805, F.Cu at (119.5, 55.0)
- added C44: 2.7n, easyeda2kicad:C0603, F.Cu at (122.2, 74.0)
- added C45: 100p, easyeda2kicad:C0402, F.Cu at (119.5, 71.0)
- added CN1: SC In, easyeda2kicad:CONN-TH_2P-P5.08_DIBO_DB128V-5.08, F.Cu at (98.5, 65.0)
- added CN2: SC Out, easyeda2kicad:CONN-TH_2P-P5.08_DIBO_DB128V-5.08, F.Cu at (138.5, 66.0)
- added H1: MountingHole_M3_3.2mm_Pad, PCM_SL_Mechanical:MountingHole_3.2mm_Pad, F.Cu at (97.5, 45.0)
- added H2: MountingHole_M3_3.2mm_Pad, PCM_SL_Mechanical:MountingHole_3.2mm_Pad, F.Cu at (139.5, 45.0)
- added H3: MountingHole_M3_3.2mm_Pad, PCM_SL_Mechanical:MountingHole_3.2mm_Pad, F.Cu at (139.5, 87.0)
- added H4: MountingHole_M3_3.2mm_Pad, PCM_SL_Mechanical:MountingHole_3.2mm_Pad, F.Cu at (97.5, 87.0)
- added L1: 3.3u, easyeda2kicad:IND-SMD_L11.5-W10.0_SMMS1040, F.Cu at (118.3, 47.0)
- added R21: 121k, easyeda2kicad:R0402, F.Cu at (114.5, 70.4)
- added R22: 8.06k, easyeda2kicad:R0603, F.Cu at (116.0, 70.8)
- added R23: 1.33k, easyeda2kicad:R0603, F.Cu at (128.2, 59.5)
- added R24: 20k, easyeda2kicad:R0603, F.Cu at (122.5, 70.8)
- added R25: 20k, easyeda2kicad:R0603, F.Cu at (124.8, 67.0)
- added R26: 2.1, easyeda2kicad:R0603, F.Cu at (112.5, 73.8)
- added U3: LM25145RGYR, easyeda2kicad:VQFN-20_L4.5-W3.5-P0.50-BL-EP, F.Cu at (119.8, 65.8)
- added U4: TP Vout, easyeda2kicad:TEST-TH_BD3.17-P1.87, F.Cu at (138.5, 75.0)
- Q1, Q2: footprint Package_SON:VSON-8_3.3x3.3mm_P0.65mm_NexFET -> easyeda2kicad:VSONP-8_L3.1-W3.1-P0.65-LS3.5-BL
- R27: value 150K_0603 -> 13k; footprint PCM_4ms_Resistor:R_0805_2012Metric -> easyeda2kicad:R0603
- R28: value 150K_0603 -> 18k; footprint PCM_4ms_Resistor:R_0805_2012Metric -> easyeda2kicad:R0603
- R29: value 150K_0603 -> 750; footprint PCM_4ms_Resistor:R_0805_2012Metric -> easyeda2kicad:R0402
- R30: value 150K_0603 -> 16.9; footprint PCM_4ms_Resistor:R_0805_2012Metric -> easyeda2kicad:R0402
- R31: value 150K_0603 -> 3.83k; footprint PCM_4ms_Resistor:R_0805_2012Metric -> easyeda2kicad:R0402
- U5: value LM25145RGYR -> TP Vin; footprint Project_Star_Regulator_Switching:RGY0020B -> easyeda2kicad:TEST-TH_BD3.17-P1.87
- U6: value LM25145RGYR -> TP GND; footprint Project_Star_Regulator_Switching:RGY0020B -> easyeda2kicad:TEST-TH_BD3.17-P1.87
- moved U6 101.8 mm to (98.5, 75.0), turned to 90 degrees
- moved U5 85.7 mm to (98.5, 56.0), turned to 90 degrees
- moved Q2 81.8 mm to (122.5, 60.0), turned to -90 degrees
- moved Q1 66.9 mm to (108.5, 71.0), turned to 90 degrees
- moved R30 64.0 mm to (131.5, 72.0), turned to -90 degrees
- moved R31 63.1 mm to (125.1, 74.0)
- moved R28 62.2 mm to (130.0, 67.5), turned to -90 degrees
- moved R29 56.9 mm to (128.4, 75.5)
- moved R27 52.9 mm to (117.5, 71.2), turned to -90 degrees
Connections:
- Q1 pad 1: Net-(Q2-D) -> Net-(U3-SW)
- Q1 pad 2: Net-(Q2-D) -> Net-(U3-SW)
- Q1 pad 3: Net-(Q2-D) -> Net-(U3-SW)
- Q2 pad 5: Net-(Q2-D) -> Net-(U3-SW)
- R27 pad 1: Net-(U5-EN_UVLO) -> Net-(U3-RT)
- R27 pad 2: /20V_Power_Line/Vin -> GND
- R28 pad 1: GND -> /20V_Power_Line/Vout
- R28 pad 2: Net-(U5-EN_UVLO) -> Net-(U3-FB)
- R29 pad 1: GND -> Net-(U3-FB)
- R29 pad 2: Net-(U5-RT) -> GND
- R30 pad 1: Net-(U5-SYNCIN) -> /20V_Power_Line/Vout
- R30 pad 2: Net-(U5-VCC) -> Net-(C41-Pad1)
- R31 pad 1: Net-(U5-PGOOD) -> Net-(C44-Pad2)
- R31 pad 2: Net-(U5-VCC) -> Net-(U3-FB)
- U5 pad 1: Net-(U5-EN_UVLO) -> /20V_Power_Line/Vin
- U6 pad 1: Net-(U6-EN_UVLO) -> GND
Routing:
- net /20V_Power_Line/Vout: track 0.00 -> 59.4 mm
- net Net-(U3-SW): track 0.00 -> 48.3 mm, vias 0 -> 2
- net /20V_Power_Line/Vin: track 0.00 -> 40.1 mm
- net Net-(U3-FB): track 0.00 -> 22.5 mm
- net Net-(U3-VCC): track 0.00 -> 20.2 mm, vias 0 -> 2
- net Net-(Q1-G): track 0.00 -> 14.1 mm
- net Net-(U3-ILIM): track 0.00 -> 13.8 mm, vias 0 -> 2
- net Net-(U3-VIN): track 0.00 -> 12.8 mm
- net Net-(U3-COMP): track 0.00 -> 7.62 mm
- net Net-(U3-SS/TRK): track 0.00 -> 7.29 mm, vias 0 -> 2
- net Net-(U3-EN/UVLO): track 0.00 -> 6.24 mm
- net Net-(U3-BST): track 0.00 -> 4.21 mm
- net Net-(C41-Pad1): track 0.00 -> 3.94 mm
- net Net-(U3-RT): track 0.00 -> 3.21 mm
- net Net-(U3-SYNCIN): track 0.00 -> 3.12 mm
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- added copper zone on B.Cu, net GND
- added copper zone on In1.Cu, net GND
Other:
- board outline added: 50 x 50 mm
- copper layers 2 -> 4
- rule pad_to_mask_clearance: 0 -> 0.05
- board text added: "20k"

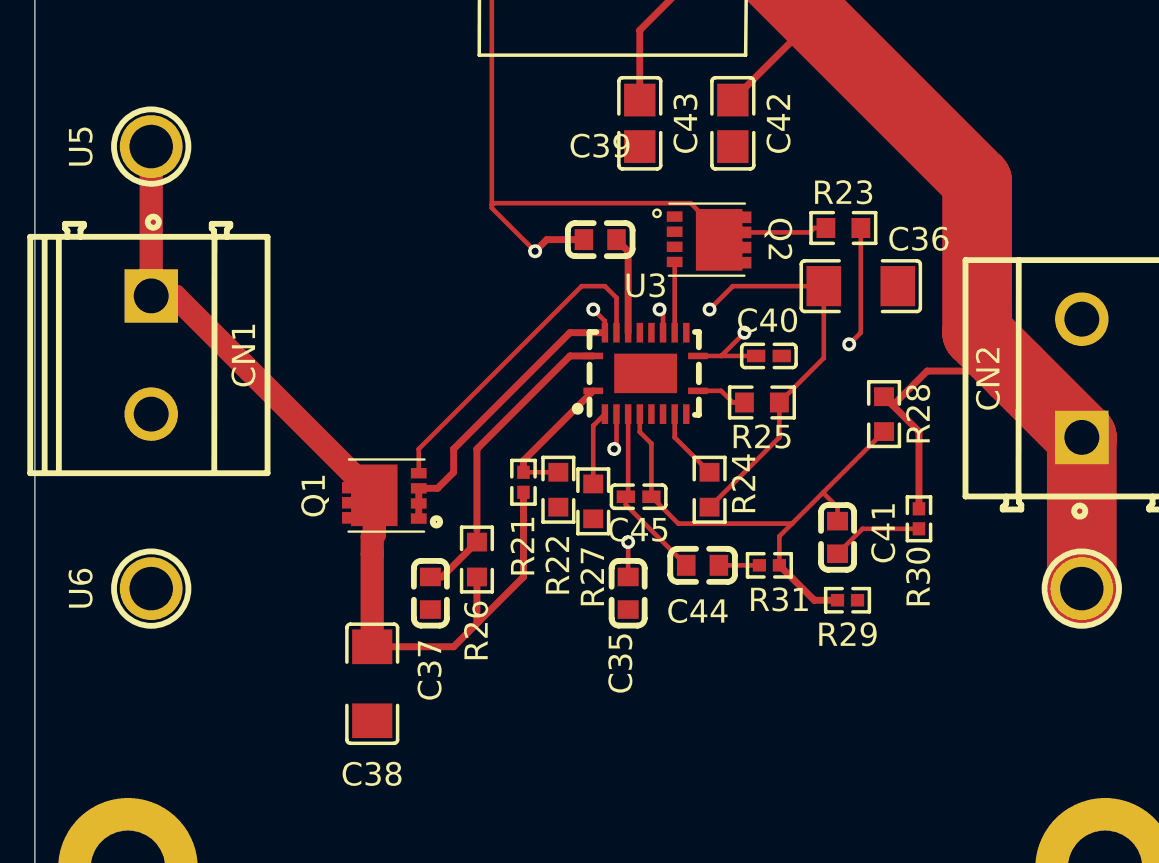
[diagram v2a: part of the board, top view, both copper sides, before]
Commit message: fixed grounding vias
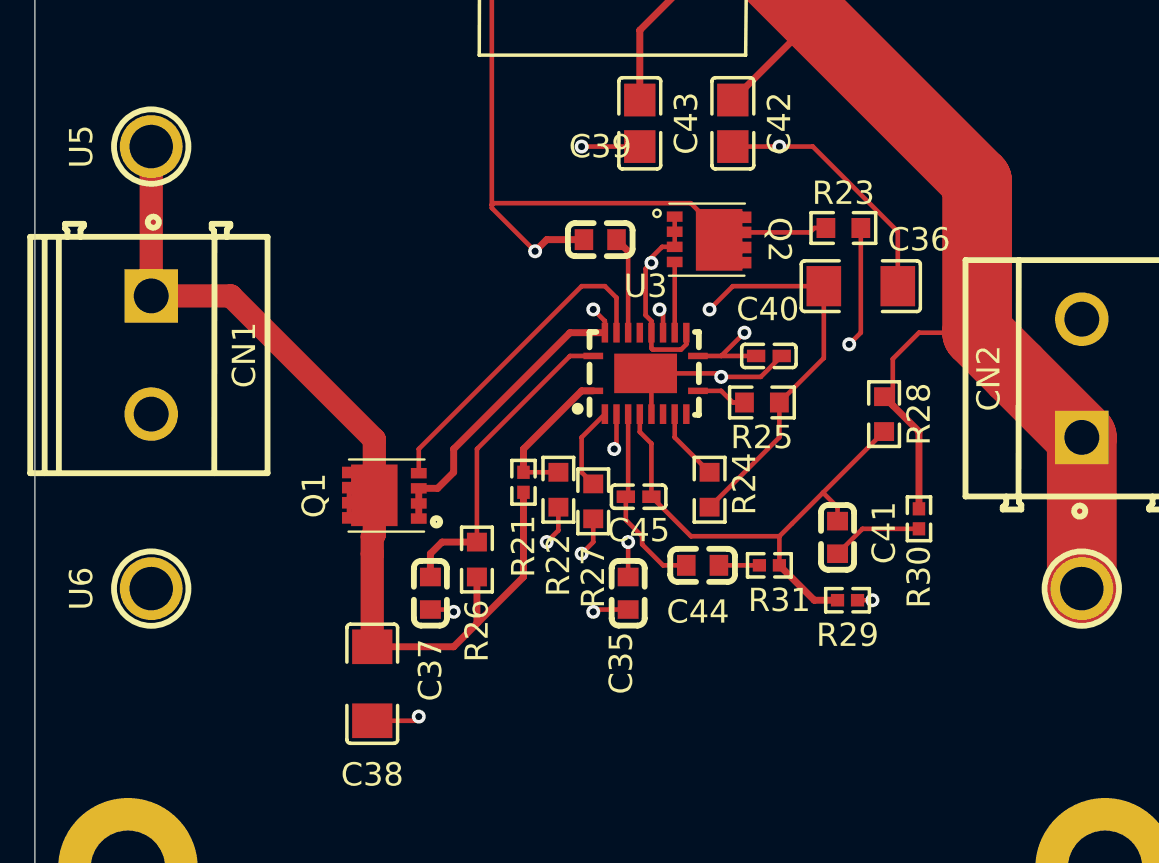
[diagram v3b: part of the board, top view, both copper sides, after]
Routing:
- net GND: track 0.00 -> 39.0 mm, vias 0 -> 10
- net /20V_Power_Line/Vin: track 40.1 -> 42.9 mm
- net Net-(U3-VIN): track 12.8 -> 13.9 mm
- net Net-(U3-COMP): track 7.62 -> 8.20 mm
- removed copper zone on In1.Cu, net GND
